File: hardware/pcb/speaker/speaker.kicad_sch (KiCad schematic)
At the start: 51 parts, among them J1 JST SH BM02B Connector, J2 JST SH BM02B Connector, J3 JST SH BM02B Connector, J4 JST SH BM02B Connector, J5 JST SH BM02B Connector, J6 JST SH BM02B Connector, J7 Conn_01x02, M1 Ultrasonic_Transducer, M10 Ultrasonic_Transducer, M11 Ultrasonic_Transducer, M12 Ultrasonic_Transducer, M13 Ultrasonic_Transducer, M14 Ultrasonic_Transducer, M15 Ultrasonic_Transducer, M16 Ultrasonic_Transducer, M17 Ultrasonic_Transducer, M18 Ultrasonic_Transducer, M19 Ultrasonic_Transducer, M2 Ultrasonic_Transducer, M3 Ultrasonic_Transducer, M4 Ultrasonic_Transducer, M5 Ultrasonic_Transducer, M6 Ultrasonic_Transducer, M7 Ultrasonic_Transducer, M8 Ultrasonic_Transducer, M9 Ultrasonic_Transducer, U1 LTC2631-Z, U2 LM2735XMF

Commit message: REWORK pcb design
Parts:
- removed JP1: Jumper_2_Open, Jumper:SolderJumper-2_P1.3mm_Bridged2Bar_Pad1.0x1.5mm, symbol Jumper:Jumper_2_Open
- added C10, C11, C8: 100nF, Capacitor_SMD:C_0805_2012Metric, symbol Device:C
- added C9: 82nF, Capacitor_SMD:C_0805_2012Metric, symbol Device:C
- added R8, R9: 15k, Resistor_SMD:R_0805_2012Metric, symbol Device:R
- C7: value 330pF -> 470pF
- L1: value 15uF -> 10uF; footprint Inductor_SMD:L_1206_3216Metric -> Inductor_SMD:L_Wuerth_5030_Handsolder; winding (none) -> .
- R4: value 5k -> 10k
- R5, R6: value 1.7k -> 1.5k
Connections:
- net +24V: now also C2.1, C7.1, D1.1 (K), R1.1, TP1.1, R8.1
- net +5V: now also L1.2, C11.1; no longer L1.1
- net Audio Sig: now also C8.1; no longer OP1.3 (+IN)
- net GND: now also C11.2, C9.1, R9.2; no longer R4.2
- net Trancducer Sig: now also C10.2; no longer OP1.1 (OUT), R3.1
- net at D1.2 (A), U2.1 (SW): now also L1.1; no longer L1.2
- new net: C8.2, OP1.3 (+IN), R8.2, R9.1
- new net: C9.2, R4.2
- new net: C10.1, OP1.1 (OUT), R3.1
- no-connect marks 0 -> 1
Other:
- moved on the sheet: C2, C3, C4, C5, C6, C7, D1, J1, J2, J3, J4, J5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

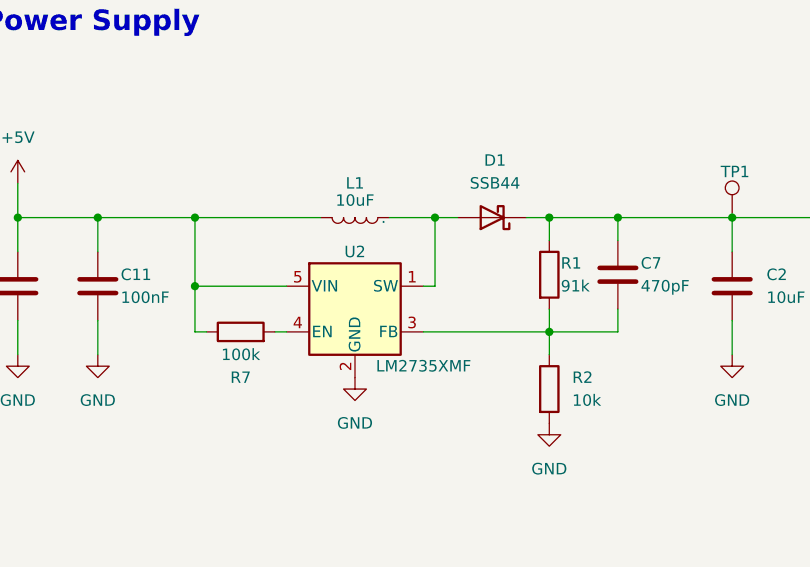
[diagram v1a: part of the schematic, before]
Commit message: REWORK pcb layout, ADD BOM
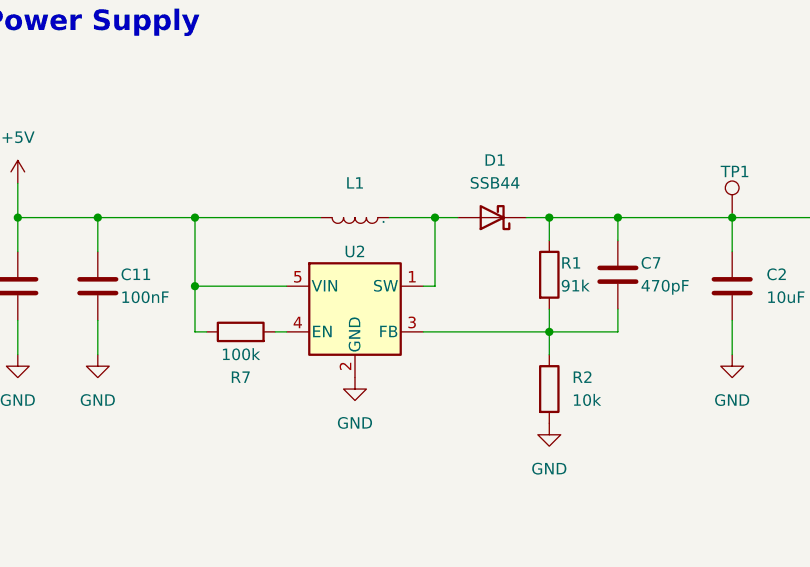
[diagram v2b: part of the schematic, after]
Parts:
- C1, C5: footprint Capacitor_SMD:C_1206_3216Metric -> Capacitor_SMD:C_1206_3216Metric_Pad1.33x1.80mm_HandSolder
- C10, C11, C4, C6, C7, C8, C9: footprint Capacitor_SMD:C_0805_2012Metric -> Capacitor_SMD:C_0805_2012Metric_Pad1.18x1.45mm_HandSolder
- C3: footprint Capacitor_SMD:C_1206_3216Metric -> Capacitor_SMD:C_0805_2012Metric_Pad1.18x1.45mm_HandSolder
- L1: value 10uF -> (none)
- R1, R2, R3, R4, R5, R6, R7, R8, R9: footprint Resistor_SMD:R_0805_2012Metric -> Resistor_SMD:R_0805_2012Metric_Pad1.20x1.40mm_HandSolder
- U2: value LM2735XMF -> (none); footprint Package_TO_SOT_SMD:SOT-23-5 -> (none)

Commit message: REV 3
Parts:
- added C12, C13: 1nF, Capacitor_SMD:C_0805_2012Metric_Pad1.18x1.45mm_HandSolder, symbol Device:C
- L1: value (none) -> 10uH
- U2: value (none) -> LM2735XMF; footprint (none) -> Package_TO_SOT_SMD:SOT-23-5_HandSoldering
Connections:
- net +24V: now also C12.1, C13.1
- net GND: now also C12.2, C13.2
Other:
- moved on the sheet: C5, C6

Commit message: update gerber files
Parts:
- R1: value 91k -> (none)
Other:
- moved on the sheet: C7
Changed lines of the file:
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@@
   (junction (at 94.615 168.91) (diameter 0) (color 0 0 0 0)
   )
-  (junction (at 102.235 43.18) (diameter 0) (color 0 0 0 0)
+  (junction (at 102.87 43.18) (diameter 0) (color 0 0 0 0)
   )
   (junction (at 145.415 160.02) (diameter 0) (color 0 0 0 0)
@@
     (stroke (width 0) (type default) (color 0 0 0 0))
   )
-  (wire (pts (xy 94.615 43.18) (xy 102.235 43.18))
+  (wire (pts (xy 94.615 43.18) (xy 102.87 43.18))
     (stroke (width 0) (type default) (color 0 0 0 0))
   )
@@
     (stroke (width 0) (type default) (color 0 0 0 0))
   )
-  (wire (pts (xy 102.235 43.18) (xy 102.235 45.72))
+  (wire (pts (xy 102.87 43.18) (xy 102.87 45.72))
     (stroke (width 0) (type default) (color 0 0 0 0))
   )
@@
     (stroke (width 0) (type default) (color 0 0 0 0))
   )
-  (wire (pts (xy 102.235 55.88) (xy 94.615 55.88))
+  (wire (pts (xy 94.615 55.88) (xy 102.87 55.88))
     (stroke (width 0) (type default) (color 0 0 0 0))
   )
@@
     (stroke (width 0) (type default) (color 0 0 0 0))
   )
-  (wire (pts (xy 102.235 53.34) (xy 102.235 55.88))
+  (wire (pts (xy 102.87 53.34) (xy 102.87 55.88))
     (stroke (width 0) (type default) (color 0 0 0 0))
   )
@@
     (stroke (width 0) (type default) (color 0 0 0 0))
   )
-  (wire (pts (xy 102.235 43.18) (xy 114.935 43.18))
+  (wire (pts (xy 102.87 43.18) (xy 114.935 43.18))
     (stroke (width 0) (type default) (color 0 0 0 0))
   )
@@
     (pin "2")
   )
-  (symbol (lib_id "Device:C") (at 102.235 49.53 0) (unit 1)
-    (in_bom yes) (on_board yes)
-    (property "Reference" "C7" (id 0) (at 104.775 48.26 0)
-      (effects (font (size 1.27 1.27)) (justify left))
-    )
-    (property "Value" "470pF" (id 1) (at 104.775 50.8 0)
-      (effects (font (size 1.27 1.27)) (justify left))
-    )
-    (property "Footprint" "Capacitor_SMD:C_0805_2012Metric_Pad1.18x1.45mm_HandSolder" (id 2) (at 103.2002 53.34 0)
-      (effects (font (size 1.27 1.27)) hide)
-    )
-    (property "Datasheet" "~" (id 3) (at 102.235 49.53 0)
+  (symbol (lib_id "Device:C") (at 102.87 49.53 0) (unit 1)
+    (in_bom yes) (on_board yes)
+    (property "Reference" "C7" (id 0) (at 105.41 48.26 0)
+      (effects (font (size 1.27 1.27)) (justify left))
+    )
+    (property "Value" "470pF" (id 1) (at 105.41 50.8 0)
+      (effects (font (size 1.27 1.27)) (justify left))
+    )
+    (property "Footprint" "Capacitor_SMD:C_0805_2012Metric_Pad1.18x1.45mm_HandSolder" (id 2) (at 103.8352 53.34 0)
+      (effects (font (size 1.27 1.27)) hide)
+    )
+    (property "Datasheet" "~" (id 3) (at 102.87 49.53 0)
       (effects (font (size 1.27 1.27)) hide)
     )
@@
       (effects (font (size 1.27 1.27)) (justify left))
     )
-    (property "Value" "91k" (id 1) (at 95.885 50.8 0)
+    (property "Value" "" (id 1) (at 95.885 50.8 0)
       (effects (font (size 1.27 1.27)) (justify left))
     )
@@
   (symbol (lib_id "power:GND") (at 128.905 57.785 0) (unit 1)
     (in_bom yes) (on_board yes) (fields_autoplaced)
-    (property "Reference" "#PWR?" (id 0) (at 128.905 64.135 0)
+    (property "Reference" "#PWR0126" (id 0) (at 128.905 64.135 0)
       (effects (font (size 1.27 1.27)) hide)
     )
@@
   (symbol (lib_id "power:GND") (at 60.96 135.89 0) (unit 1)
     (in_bom yes) (on_board yes)
-    (property "Reference" "#PWR?" (id 0) (at 60.96 142.24 0)
+    (property "Reference" "#PWR0127" (id 0) (at 60.96 142.24 0)
       (effects (font (size 1.27 1.27)) hide)
     )
@@
     )
     (path "/98c4b092-bf78-43ca-8d74-941c15d8fe89"
-      (reference "#PWR?") (unit 1) (value "GND") (footprint "")
+      (reference "#PWR0126") (unit 1) (value "GND") (footprint "")
     )
     (path "/a091b038-73b8-4e3d-85bf-957d7c13689e"
-      (reference "#PWR?") (unit 1) (value "GND") (footprint "")
+      (reference "#PWR0127") (unit 1) (value "GND") (footprint "")
     )
     (path "/de384e4c-069b-4b07-a4c3-77b810d8d24d"
@@
     )
     (path "/61a54c8a-9e28-4416-b95f-f6b26668dc82"
-      (reference "R1") (unit 1) (value "91k") (footprint "Resistor_SMD:R_0805_2012Metric_Pad1.20x1.40mm_HandSolder")
+      (reference "R1") (unit 1) (value "180k") (footprint "Resistor_SMD:R_0805_2012Metric_Pad1.20x1.40mm_HandSolder")
     )
     (path "/b85e5a65-f482-4007-af41-df630a532e20"

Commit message: update gerber files
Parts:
- OP1: value ADA4622-1 -> (none); footprint Package_TO_SOT_SMD:SOT-23-5_HandSoldering -> (none); symbol custom_symbols:ADA4622-1 -> custom_symbols:TL081H_DBV
- R1: value (none) -> 180k
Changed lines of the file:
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@@
       (effects (font (size 1.27 1.27)) (justify left))
     )
-    (property "Value" "" (id 1) (at 95.885 50.8 0)
+    (property "Value" "180k" (id 1) (at 95.885 50.8 0)
       (effects (font (size 1.27 1.27)) (justify left))
     )
@@
     (pin "1")
   )
-  (symbol (lib_id "custom_symbols:ADA4622-1") (at 55.88 149.86 0) (unit 1)
+  (symbol (lib_id "custom_symbols:TL081H_DBV") (at 55.88 149.86 0) (unit 1)
     (in_bom yes) (on_board yes)
     (property "Reference" "OP1" (id 0) (at 59.69 143.51 0))
-    (property "Value" "ADA4622-1" (id 1) (at 63.5 146.05 0))
-    (property "Footprint" "Package_TO_SOT_SMD:SOT-23-5_HandSoldering" (id 2) (at 55.88 149.86 0)
-      (effects (font (size 1.27 1.27)) hide)
-    )
+    (property "Value" "" (id 1) (at 63.5 146.05 0))
+    (property "Footprint" "" (id 2) (at 55.88 149.86 0)
+      (effects (font (size 1.27 1.27)) hide)
+    )
